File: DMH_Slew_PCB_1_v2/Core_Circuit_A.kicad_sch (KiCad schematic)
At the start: 52 parts, among them J1 TS_Jack_6.35mm_Sw, J2 TS_Jack_6.35mm_Sw, J3 TS_Jack_6.35mm_Sw, J50 Conn_01x08_PinHeader, J51 Conn_01x08_PinHeader, Q1 BC548, Q2 BC548, Q3 BC558, Q4 BC558, SW1 SW_DPDT_3way, SW2 SW_DPDT, SW3 SPDT_OnOffOn, U1 TL074, U2 TL074

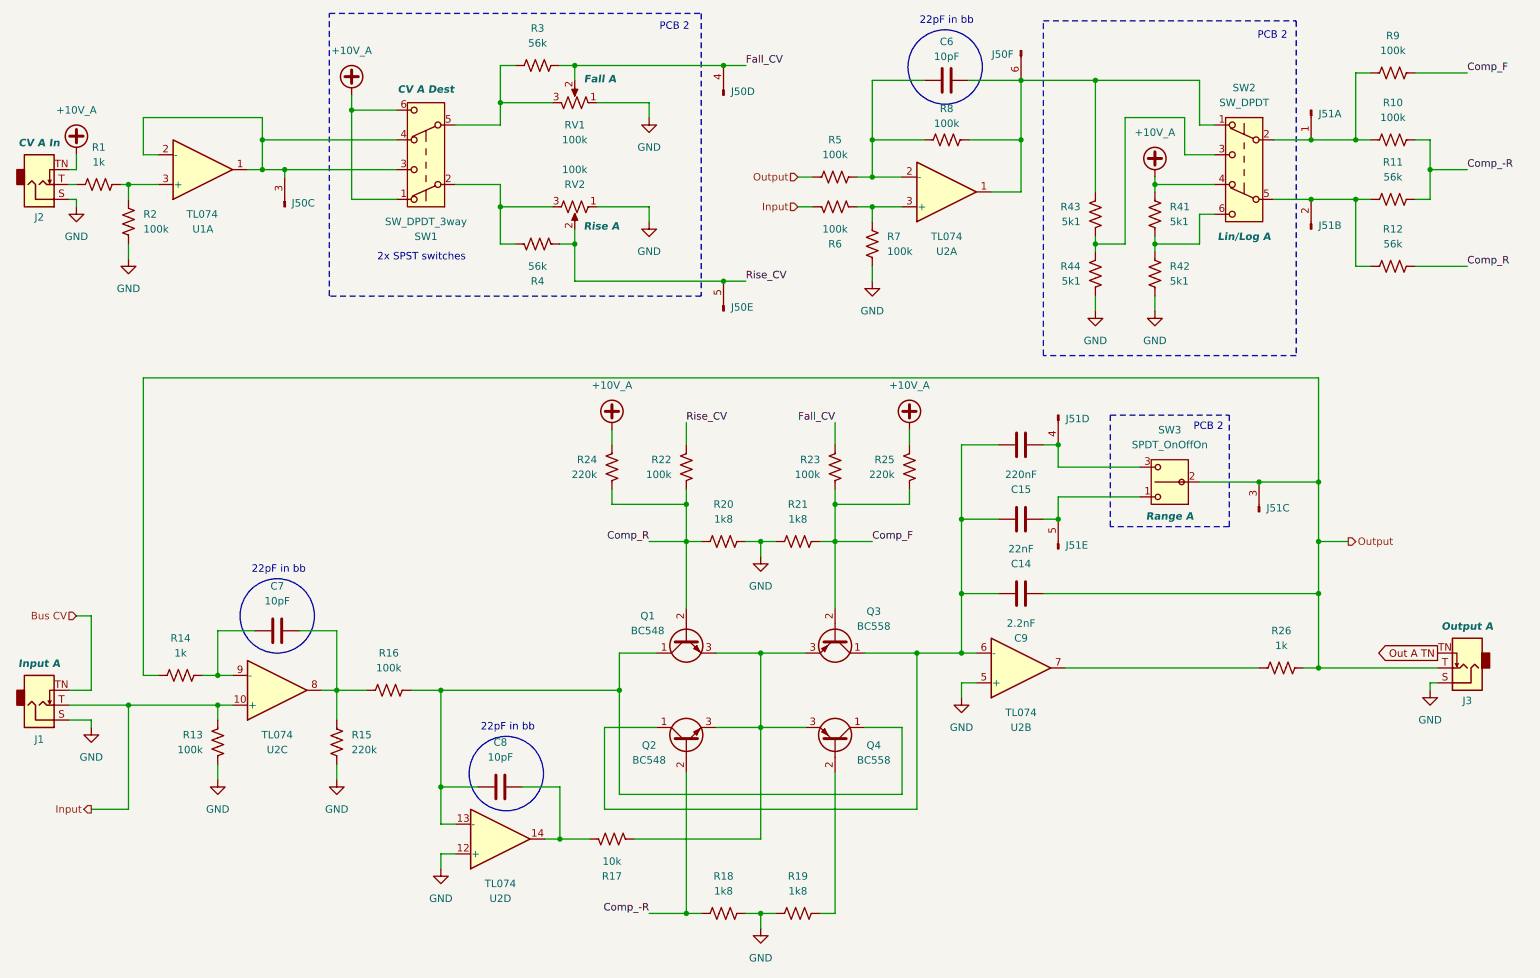
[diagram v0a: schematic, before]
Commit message: PCB 2 component placement done
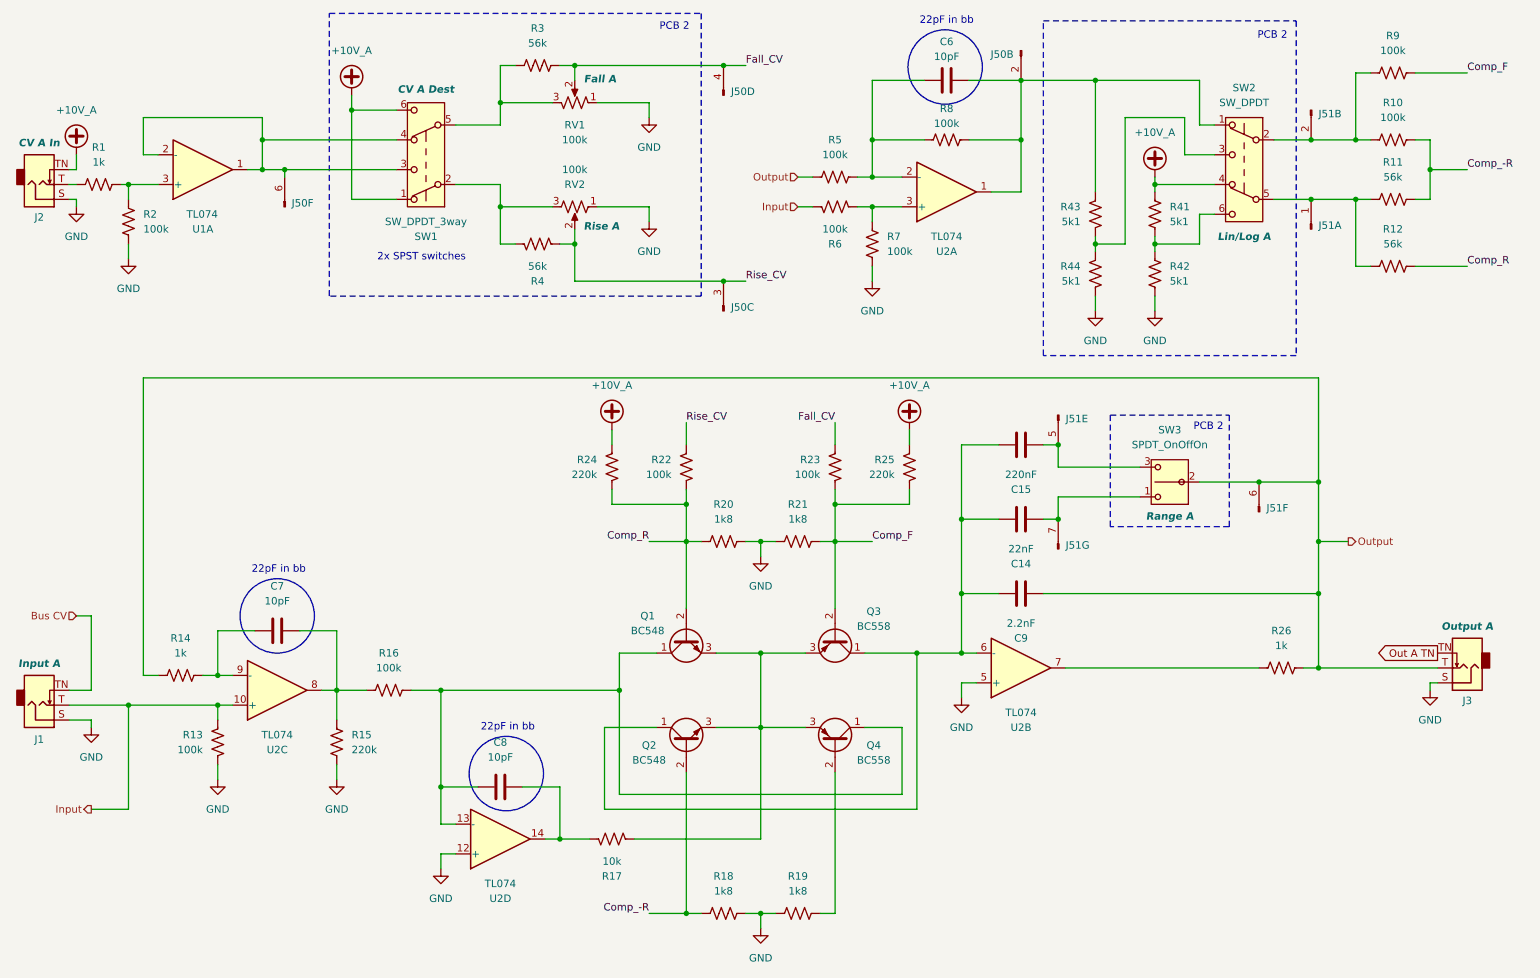
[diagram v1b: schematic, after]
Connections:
- net Output: now also J51.6 (Pin_6); no longer J51.3 (Pin_3)
- net Rise_CV: now also J50.3 (Pin_3); no longer J50.5 (Pin_5)
- net at C6.2, R43.1, R8.1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: now also J50.2 (Pin_2); no longer J50.6 (Pin_6)
- net at C15.2, SW3.3 (C): now also J51.5 (Pin_5); no longer J51.4 (Pin_4)
- net at R11.2, R12.2, SW2.5 (B): now also J51.1 (Pin_1); no longer J51.2 (Pin_2)
- net at SW1.3 (C), SW1.4 (A), U1.1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: now also J50.6 (Pin_6); no longer J50.3 (Pin_3)
- net at R10.2, R9.2, SW2.2 (B): now also J51.2 (Pin_2); no longer J51.1 (Pin_1)
- net at C14.2, SW3.1 (A): now also J51.7 (Pin_7); no longer J51.5 (Pin_5)
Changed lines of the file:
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@@
 		(at 190.5 30.48 90)
 		(mirror x)
-		(unit 6)
+		(unit 2)
 		(exclude_from_sim no)
 		(in_bom yes)
@@
 				(path "/58f4306d-5387-4983-bb08-41a2313fd315/7ad2d702-dfb7-4d49-a82d-34430dd5948f"
 					(reference "J50")
-					(unit 6)
+					(unit 2)
 				)
 			)
@@
 		(lib_id "SynthStuff:Conn_01x08_PinHeader")
 		(at 240.03 60.96 90)
-		(unit 2)
+		(unit 1)
 		(exclude_from_sim no)
 		(in_bom yes)
@@
 				(path "/58f4306d-5387-4983-bb08-41a2313fd315/7ad2d702-dfb7-4d49-a82d-34430dd5948f"
 					(reference "J51")
-					(unit 2)
+					(unit 1)
 				)
 			)
@@
 		(lib_id "SynthStuff:Conn_01x08_PinHeader")
 		(at 231.14 109.22 90)
-		(unit 3)
+		(unit 6)
 		(exclude_from_sim no)
 		(in_bom yes)
@@
 				(path "/58f4306d-5387-4983-bb08-41a2313fd315/7ad2d702-dfb7-4d49-a82d-34430dd5948f"
 					(reference "J51")
-					(unit 3)
+					(unit 6)
 				)
 			)
@@
 		(lib_id "SynthStuff:Conn_01x08_PinHeader")
 		(at 196.85 115.57 90)
-		(unit 5)
+		(unit 7)
 		(exclude_from_sim no)
 		(in_bom yes)
@@
 				(path "/58f4306d-5387-4983-bb08-41a2313fd315/7ad2d702-dfb7-4d49-a82d-34430dd5948f"
 					(reference "J51")
-					(unit 5)
+					(unit 7)
 				)
 			)
@@
 		(lib_id "SynthStuff:Conn_01x08_PinHeader")
 		(at 64.77 57.15 90)
-		(unit 3)
+		(unit 6)
 		(exclude_from_sim no)
 		(in_bom yes)
@@
 				(path "/58f4306d-5387-4983-bb08-41a2313fd315/7ad2d702-dfb7-4d49-a82d-34430dd5948f"
 					(reference "J50")
-					(unit 3)
+					(unit 6)
 				)
 			)
@@
 		(lib_id "SynthStuff:Conn_01x08_PinHeader")
 		(at 196.85 92.71 270)
-		(unit 4)
+		(unit 5)
 		(exclude_from_sim no)
 		(in_bom yes)
@@
 				(path "/58f4306d-5387-4983-bb08-41a2313fd315/7ad2d702-dfb7-4d49-a82d-34430dd5948f"
 					(reference "J51")
-					(unit 4)
+					(unit 5)
 				)
 			)
@@
 		(lib_id "SynthStuff:Conn_01x08_PinHeader")
 		(at 240.03 40.64 270)
-		(unit 1)
+		(unit 2)
 		(exclude_from_sim no)
 		(in_bom yes)
@@
 				(path "/58f4306d-5387-4983-bb08-41a2313fd315/7ad2d702-dfb7-4d49-a82d-34430dd5948f"
 					(reference "J51")
-					(unit 1)
+					(unit 2)
 				)
 			)
@@
 		(lib_id "SynthStuff:Conn_01x08_PinHeader")
 		(at 139.7 74.93 90)
-		(unit 5)
+		(unit 3)
 		(exclude_from_sim no)
 		(in_bom yes)
@@
 				(path "/58f4306d-5387-4983-bb08-41a2313fd315/7ad2d702-dfb7-4d49-a82d-34430dd5948f"
 					(reference "J50")
-					(unit 5)
+					(unit 3)
 				)
 			)

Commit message: PCB 1 component placement ongoing
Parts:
- Q2, Q4: footprint Package_TO_SOT_THT:TO-92_Inline -> Package_TO_SOT_THT:TO-92L_Inline_Wide
- U1: footprint Package_DIP:DIP-16_W7.62mm_Socket -> Package_DIP:DIP-14_W7.62mm_Socket
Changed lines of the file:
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@@
 			)
 		)
-		(property "Footprint" "Package_TO_SOT_THT:TO-92_Inline"
+		(property "Footprint" "Package_TO_SOT_THT:TO-92L_Inline_Wide"
 			(at 156.845 143.51 0)
 			(effects
@@
 			)
 		)
-		(property "Footprint" "Package_TO_SOT_THT:TO-92_Inline"
+		(property "Footprint" "Package_TO_SOT_THT:TO-92L_Inline_Wide"
 			(at 135.255 143.51 0)
 			(effects
@@
 			)
 		)
-		(property "Footprint" "Package_DIP:DIP-16_W7.62mm_Socket"
+		(property "Footprint" "Package_DIP:DIP-14_W7.62mm_Socket"
 			(at 49.53 53.34 0)
 			(effects

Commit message: Updated Log circuit
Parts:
- removed R41, R42, R43, R44: 5k1, Resistor_THT:R_Axial_DIN0207_L6.3mm_D2.5mm_P7.62mm_Horizontal, symbol Device:R_US
- R11, R12: value 56k -> 100k
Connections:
- net GND: now also SW2.3 (C), SW2.6 (C)
